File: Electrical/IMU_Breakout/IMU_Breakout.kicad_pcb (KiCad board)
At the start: 2 copper layers, 26.5 x 23.9 mm, 9 parts, among them J1 Conn_01x04_Pin, J2 Conn_01x04_Pin, U1 BMI323

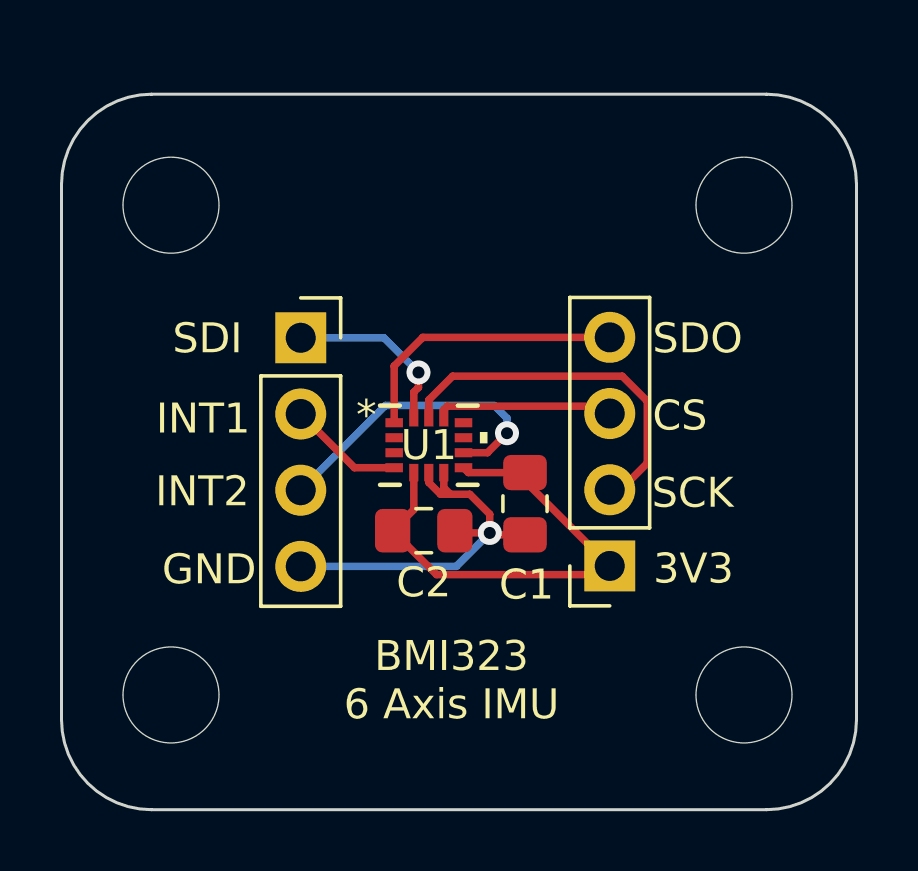
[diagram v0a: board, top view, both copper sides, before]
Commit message: Center the IMU
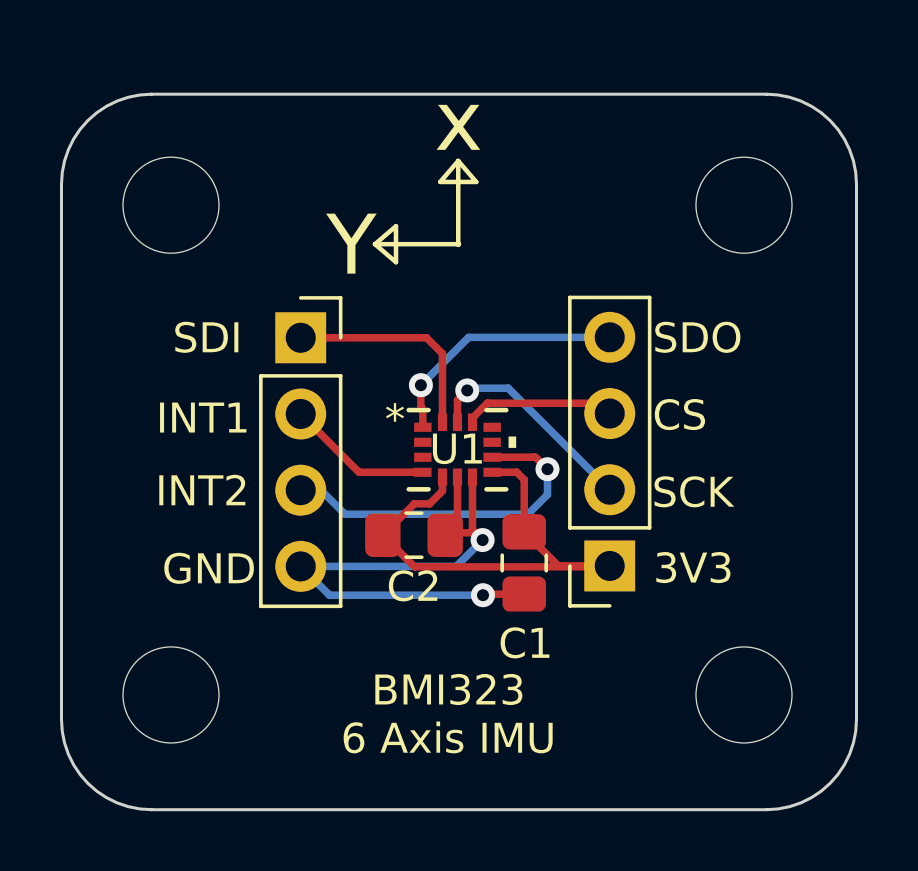
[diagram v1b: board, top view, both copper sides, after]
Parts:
- moved C1 1.98 mm to (232.6, 128.1)
- moved U1 0.97 mm to (230.3, 124.3)
- moved C2 0.36 mm to (228.9, 127.2)
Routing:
- net GND: track 13.3 -> 19.3 mm, vias 1 -> 2
- net Net-(J2-Pin_2): track 12.3 -> 7.38 mm, vias 0 -> 1
- net Net-(J1-Pin_1): track 5.98 -> 7.23 mm, vias 1 -> 0
- net Net-(J1-Pin_2): track 3.86 -> 4.87 mm
- net Net-(J2-Pin_3): track 5.39 -> 4.44 mm
- net Net-(J2-Pin_4): track 9.26 -> 8.38 mm, vias 0 -> 1
- net +3.3V: track 16.4 -> 17.1 mm
- net Net-(J1-Pin_3): track 10.4 -> 11.0 mm
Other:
- board text added: "Hole spacing: 19.1 mm x 16.325 mm Board Size: 26.5 mm x 23.875 mm"
- board text added: "Y"
- board text added: "x"

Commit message: Finalize IMU Breakout board
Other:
- board text added: "Board Size: 26.5 mm x 23.875 mm"
- board text added: "Hole spacing: 19.1 mm x 16.325 mm"
- board text added: "Z"
- board text removed: "Hole spacing: 19.1 mm x 16.325 mm Board Size: 26.5 mm x 23.875 mm"
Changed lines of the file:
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@@
       (outputformat 1)
       (mirror false)
-      (drillshape 1)
+      (drillshape 0)
       (scaleselection 1)
-      (outputdirectory "")
+      (outputdirectory "gerbers/")
     )
   )
@@
     (fp_line (start 1 0.625) (end -1 0.625)
       (stroke (width 0.1) (type solid)) (layer "F.Fab"))
-    (pad "1" smd roundrect (at -1.0375 0 270) (size 1.175 1.45) (layers "F.Cu" "F.Paste" "F.Mask") (roundrect_rratio 0.212766)
+    (pad "1" smd roundrect (at -1.0375 0 270) (size 1.175 1.45) (layers "F.Cu" "F.Paste" "F.Mask") (roundrect_rratio 0.2127659574)
       (net 1 "+3.3V") (pintype "passive"))
-    (pad "2" smd roundrect (at 1.0375 0 270) (size 1.175 1.45) (layers "F.Cu" "F.Paste" "F.Mask") (roundrect_rratio 0.212766)
+    (pad "2" smd roundrect (at 1.0375 0 270) (size 1.175 1.45) (layers "F.Cu" "F.Paste" "F.Mask") (roundrect_rratio 0.2127659574)
       (net 2 "GND") (pintype "passive"))
     (model "${KICAD6_3DMODEL_DIR}/Capacitor_SMD.3dshapes/C_0805_2012Metric.wrl"
@@
     (fp_line (start 1 0.625) (end -1 0.625)
       (stroke (width 0.1) (type solid)) (layer "F.Fab"))
-    (pad "1" smd roundrect (at -1.0375 0) (size 1.175 1.45) (layers "F.Cu" "F.Paste" "F.Mask") (roundrect_rratio 0.212766)
+    (pad "1" smd roundrect (at -1.0375 0) (size 1.175 1.45) (layers "F.Cu" "F.Paste" "F.Mask") (roundrect_rratio 0.2127659574)
       (net 1 "+3.3V") (pintype "passive"))
-    (pad "2" smd roundrect (at 1.0375 0) (size 1.175 1.45) (layers "F.Cu" "F.Paste" "F.Mask") (roundrect_rratio 0.212766)
+    (pad "2" smd roundrect (at 1.0375 0) (size 1.175 1.45) (layers "F.Cu" "F.Paste" "F.Mask") (roundrect_rratio 0.2127659574)
       (net 2 "GND") (pintype "passive"))
     (model "${KICAD6_3DMODEL_DIR}/Capacitor_SMD.3dshapes/C_0805_2012Metric.wrl"
@@
     (pad "" np_thru_hole circle (at 0 0) (size 3.2 3.2) (drill 3.2) (layers "*.Cu" "*.Mask"))
   )
+  (gr_line (start 228.21 123.68) (end 227.51 124.28)
+    (stroke (width 0.15) (type default)) (layer "B.SilkS"))
+  (gr_line (start 229.71 122.24) (end 230.91 122.24)
+    (stroke (width 0.15) (type default)) (layer "B.SilkS"))
+  (gr_line (start 230.31 121.54) (end 230.31 124.34)
+    (stroke (width 0.15) (type default)) (layer "B.SilkS"))
+  (gr_line (start 229.71 122.24) (end 230.31 121.54)
+    (stroke (width 0.15) (type default)) (layer "B.SilkS"))
+  (gr_line (start 228.21 124.88) (end 227.51 124.28)
+    (stroke (width 0.15) (type default)) (layer "B.SilkS"))
+  (gr_line (start 228.21 124.88) (end 228.21 123.68)
+    (stroke (width 0.15) (type default)) (layer "B.SilkS"))
+  (gr_line (start 227.51 124.28) (end 230.31 124.28)
+    (stroke (width 0.15) (type default)) (layer "B.SilkS"))
+  (gr_line (start 230.91 122.24) (end 230.31 121.54)
+    (stroke (width 0.15) (type default)) (layer "B.SilkS"))
+  (gr_line (start 230.61 124.62) (end 230 123.98)
+    (stroke (width 0.15) (type default)) (layer "B.SilkS"))
+  (gr_line (start 230.03 124.65) (end 230.63 123.96)
+    (stroke (width 0.15) (type default)) (layer "B.SilkS"))
   (gr_line (start 229.75 115.375) (end 230.95 115.375)
     (stroke (width 0.15) (type default)) (layer "F.SilkS"))
@@
   (gr_line (start 230.375 117.45) (end 227.575 117.45)
     (stroke (width 0.15) (type default)) (layer "F.SilkS"))
+  (gr_circle (center 230.375 117.45) (end 230.745 117.7)
+    (stroke (width 0.15) (type default)) (fill none) (layer "F.SilkS"))
   (gr_line (start 230.35 114.675) (end 230.95 115.375)
     (stroke (width 0.15) (type default)) (layer "F.SilkS"))
@@
     (effects (font (size 1 1) (thickness 0.15)) (justify left bottom mirror))
   )
-  (gr_text "Hole spacing:\n19.1 mm x 16.325 mm\n\nBoard Size:\n26.5 mm x 23.875 mm" (at 233.925 115.5 90) (layer "B.SilkS")
+  (gr_text "Hole spacing:\n19.1 mm x \n16.325 mm\n" (at 235.29 117.67) (layer "B.SilkS")
     (effects (font (size 1 1) (thickness 0.15)) (justify left bottom mirror))
   )
@@
     (effects (font (size 1 1) (thickness 0.15)) (justify left bottom mirror))
   )
+  (gr_text "Y" (at 229.04 127.19) (layer "B.SilkS")
+    (effects (font (size 2 2) (thickness 0.15)) (justify left bottom mirror))
+  )
   (gr_text "3V3" (at 239.75 128.9) (layer "B.SilkS")
     (effects (font (size 1 1) (thickness 0.15)) (justify left bottom mirror))
   )
+  (gr_text "x" (at 231.11 121.415) (layer "B.SilkS")
+    (effects (font (size 2 2) (thickness 0.15)) (justify left bottom mirror))
+  )
   (gr_text "INT2" (at 223.872618 126.225) (layer "B.SilkS")
     (effects (font (size 1 1) (thickness 0.15)) (justify left bottom mirror))
   )
   (gr_text "GND" (at 223.647618 128.825) (layer "B.SilkS")
+    (effects (font (size 1 1) (thickness 0.15)) (justify left bottom mirror))
+  )
+  (gr_text "Z" (at 232.27 126.24) (layer "B.SilkS")
+    (effects (font (size 1.5 1.5) (thickness 0.15)) (justify left bottom mirror))
+  )
+  (gr_text "Board Size:\n26.5 mm x \n23.875 mm" (at 234.14 135.26) (layer "B.SilkS")
     (effects (font (size 1 1) (thickness 0.15)) (justify left bottom mirror))
   )
@@
   (gr_text "3V3" (at 236.85 128.85) (layer "F.SilkS")
     (effects (font (size 1 1) (thickness 0.15)) (justify left bottom))
+  )
+  (gr_text "Z" (at 230.83 118.47) (layer "F.SilkS")
+    (effects (font (size 1.5 1.5) (thickness 0.15)) (justify left bottom))
   )
   (gr_text "BMI323 \n6 Axis IMU" (at 230.025 134.525) (layer "F.SilkS")
@@
   (segment (start 227.8375 127.15) (end 228.8923 128.2048) (width 0.25) (layer "F.Cu") (net 1))
   (segment (start 232.55 125.3) (end 232.300001 125.050001) (width 0.25) (layer "F.Cu") (net 1))
-  (segment (start 230.824999 125.2144) (end 230.824999 126.974999) (width 0.25) (layer "F.Cu") (net 2))
-  (segment (start 230.824999 126.974999) (end 231.1625 127.3125) (width 0.25) (layer "F.Cu") (net 2))
+  (segment (start 231.15 127.4851) (end 231.16 127.4751) (width 0.25) (layer "F.Cu") (net 2))
+  (segment (start 230.7399 127.075) (end 230.3125 127.075) (width 0.25) (layer "F.Cu") (net 2))
+  (segment (start 231.15 127.4851) (end 230.7399 127.075) (width 0.25) (layer "F.Cu") (net 2))
   (segment (start 232.55 129.1125) (end 231.2125 129.1125) (width 0.25) (layer "F.Cu") (net 2))
-  (segment (start 230.925 127.075) (end 230.3125 127.075) (width 0.25) (layer "F.Cu") (net 2))
+  (segment (start 230.824999 125.4792) (end 230.824999 125.2144) (width 0.25) (layer "F.Cu") (net 2))
+  (segment (start 231.16 125.814201) (end 230.824999 125.4792) (width 0.25) (layer "F.Cu") (net 2))
   (segment (start 231.2125 129.1125) (end 231.175 129.15) (width 0.25) (layer "F.Cu") (net 2))
-  (segment (start 231.1625 127.3125) (end 230.925 127.075) (width 0.25) (layer "F.Cu") (net 2))
+  (segment (start 231.16 127.4751) (end 231.16 125.814201) (width 0.25) (layer "F.Cu") (net 2))
   (segment (start 230.325 127.0625) (end 230.325 125.2144) (width 0.25) (layer "F.Cu") (net 2))
   (via (at 231.175 129.15) (size 0.8) (drill 0.4) (layers "F.Cu" "B.Cu") (net 2))
-  (via (at 231.1625 127.3125) (size 0.8) (drill 0.4) (layers "F.Cu" "B.Cu") (net 2))
-  (segment (start 230.285 128.19) (end 225.1 128.19) (width 0.25) (layer "B.Cu") (net 2))
-  (segment (start 231.1625 127.3125) (end 230.285 128.19) (width 0.25) (layer "B.Cu") (net 2))
+  (via (at 231.15 127.4851) (size 0.8) (drill 0.4) (layers "F.Cu" "B.Cu") (net 2))
   (segment (start 226.06 129.15) (end 225.1 128.19) (width 0.25) (layer "B.Cu") (net 2))
+  (segment (start 231.15 127.4851) (end 230.4451 128.19) (width 0.25) (layer "B.Cu") (net 2))
+  (segment (start 230.4451 128.19) (end 225.1 128.19) (width 0.25) (layer "B.Cu") (net 2))
   (segment (start 231.175 129.15) (end 226.06 129.15) (width 0.25) (layer "B.Cu") (net 2))
   (segment (start 227.040001 125.050001) (end 229.1693 125.050001) (width 0.25) (layer "F.Cu") (net 3))
@@
   (segment (start 229.105301 122.15) (end 230.700301 120.555) (width 0.25) (layer "B.Cu") (net 12))
   (segment (start 230.700301 120.555) (end 235.4 120.555) (width 0.25) (layer "B.Cu") (net 12))
+  (group "" (id 6b63ddff-342a-4103-9e80-566f4ca48f87)
+    (members
+      0e9e0b69-7654-41b2-a422-72601af4242d
+      6da0fa1d-0137-40cc-b95d-b93eec7d2244
+      79c8b74f-e240-4118-b2b8-ac3ac8559dcf
+      b618bfb6-58a1-4f99-83a7-837fc45daef0
+      d9c547ea-17e5-4faf-942d-de3d7201395e
+    )
+  )
+  (group "" (id f9f491da-1c0c-4b05-a07e-3ad74f8c2366)
+    (members
+      1d0dc823-193f-46a7-894e-c925dc06a309
+      3ea3d6cc-a477-4565-b0fd-0dfb934883da
+      5b45e2c5-9f41-4e3a-8621-c51958769b5f
+      b7a7c98f-c956-4b69-bcce-ce541e4ed3b7
+      dc3b5726-1f00-4d6f-955f-c443f1eba916
+    )
+  )
   (group "" (id 564185dc-e40a-4285-baaa-7e9a44a39207)
     (members

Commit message: Finalize the PCBs
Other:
- board text added: "BOTTOM"
- board text added: "TOP"

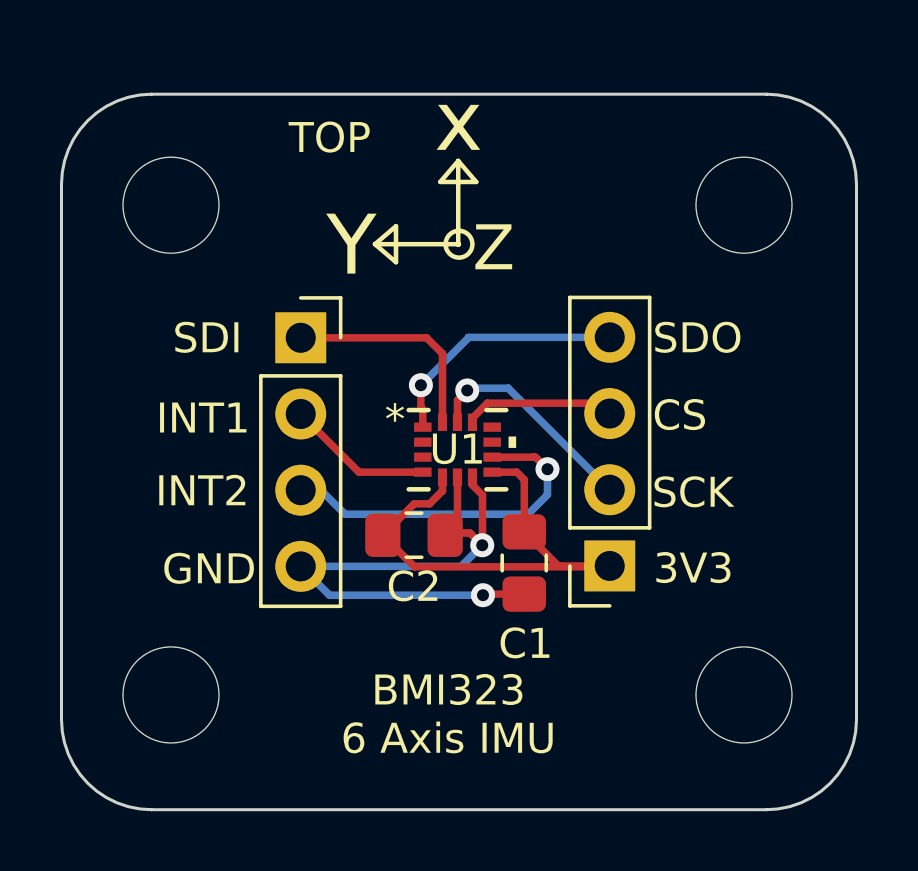
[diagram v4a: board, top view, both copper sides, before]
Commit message: Update the connection for IMU breakout board
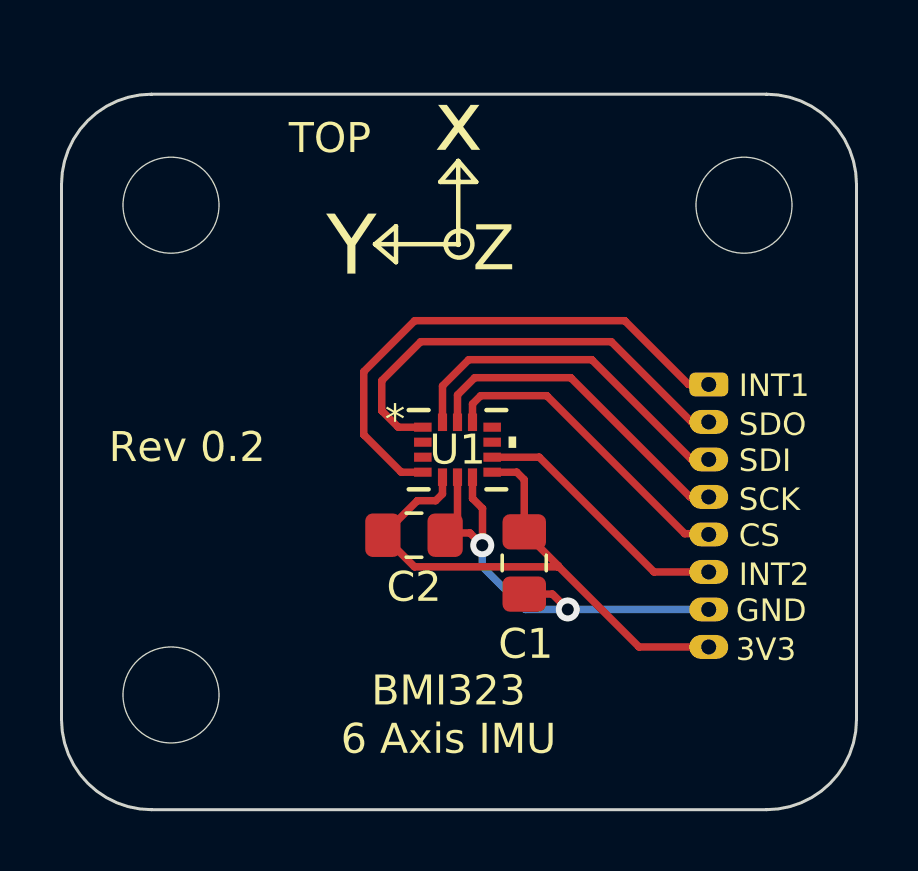
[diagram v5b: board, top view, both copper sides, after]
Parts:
- removed H3: MountingHole, MountingHole:MountingHole_3.2mm_M3
- removed J1, J2: Conn_01x04_Pin, Connector_PinSocket_2.54mm:PinSocket_1x04_P2.54mm_Vertical
- added J3: Conn_01x08_Pin, Connector_Molex:Molex_PicoBlade_53048-0810_1x08_P1.25mm_Horizontal, B.Cu at (238.7, 122.1)
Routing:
- net Net-(J3-Pin_1): track 4.87 -> 17.7 mm
- net Net-(J3-Pin_2): track 8.38 -> 15.1 mm, vias 1 -> 0
- net Net-(J3-Pin_5): track 4.44 -> 10.5 mm
- net Net-(J3-Pin_3): track 7.23 -> 11.8 mm
- net Net-(J3-Pin_4): track 7.38 -> 11.2 mm, vias 1 -> 0
- net GND: track 19.5 -> 15.8 mm
- net +3.3V: track 17.1 -> 20.1 mm
- net Net-(J3-Pin_6): track 11.0 -> 8.80 mm, vias 1 -> 0
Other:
- board text added: "Rev 0.2"
